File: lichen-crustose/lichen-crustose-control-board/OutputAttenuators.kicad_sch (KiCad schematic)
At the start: 10 parts, among them J7 Thonkiconn_Mono_Audio_Jack, J8 Thonkiconn_Mono_Audio_Jack

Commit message: Updates Lichen symbols and footprints. Fixes to Crustose and Vactrol VCA. Adds 3D model of the RP2350 dual USB board.
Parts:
- J7, J8, RV9: now left out of the parts list
- R33, R34: value 10k_0603 -> 1k_0603; JLCPCB ID C25804 -> (none)
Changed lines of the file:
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@@
 			)
 		)
-		(property "Datasheet" ""
+		(property "Datasheet" "https://jlcpcb.com/api/file/downloadByFileSystemAccessId/8579706381320323072"
 			(at 91.44 82.55 0)
 			(effects
@@
 		(unit 1)
 		(exclude_from_sim no)
-		(in_bom yes)
+		(in_bom no)
 		(on_board yes)
 		(dnp no)
@@
 			)
 		)
-		(property "Value" "10k_0603"
+		(property "Value" "1k_0603"
 			(at 97.79 133.35 90)
 			(effects
@@
 			)
 		)
-		(property "JLCPCB ID" "C25804"
-			(at 113.03 137.16 0)
-			(effects
-				(font
-					(size 1.27 1.27)
-				)
-				(hide yes)
-			)
-		)
 		(property "LCSC" "C21190"
 			(at 115.824 137.16 0)
@@
 		(unit 1)
 		(exclude_from_sim no)
-		(in_bom yes)
+		(in_bom no)
 		(on_board yes)
 		(dnp no)
@@
 			)
 		)
-		(property "Datasheet" ""
+		(property "Datasheet" "https://jlcpcb.com/api/file/downloadByFileSystemAccessId/8579706381320323072"
 			(at 91.44 123.19 0)
 			(effects
@@
 		(unit 1)
 		(exclude_from_sim no)
-		(in_bom yes)
+		(in_bom no)
 		(on_board yes)
 		(dnp no)
@@
 			)
 		)
-		(property "Value" "10k_0603"
+		(property "Value" "1k_0603"
 			(at 96.52 92.71 90)
 			(effects
@@
 			)
 		)
-		(property "JLCPCB ID" "C25804"
-			(at 111.76 96.52 0)
-			(effects
-				(font
-					(size 1.27 1.27)
-				)
-				(hide yes)
-			)
-		)

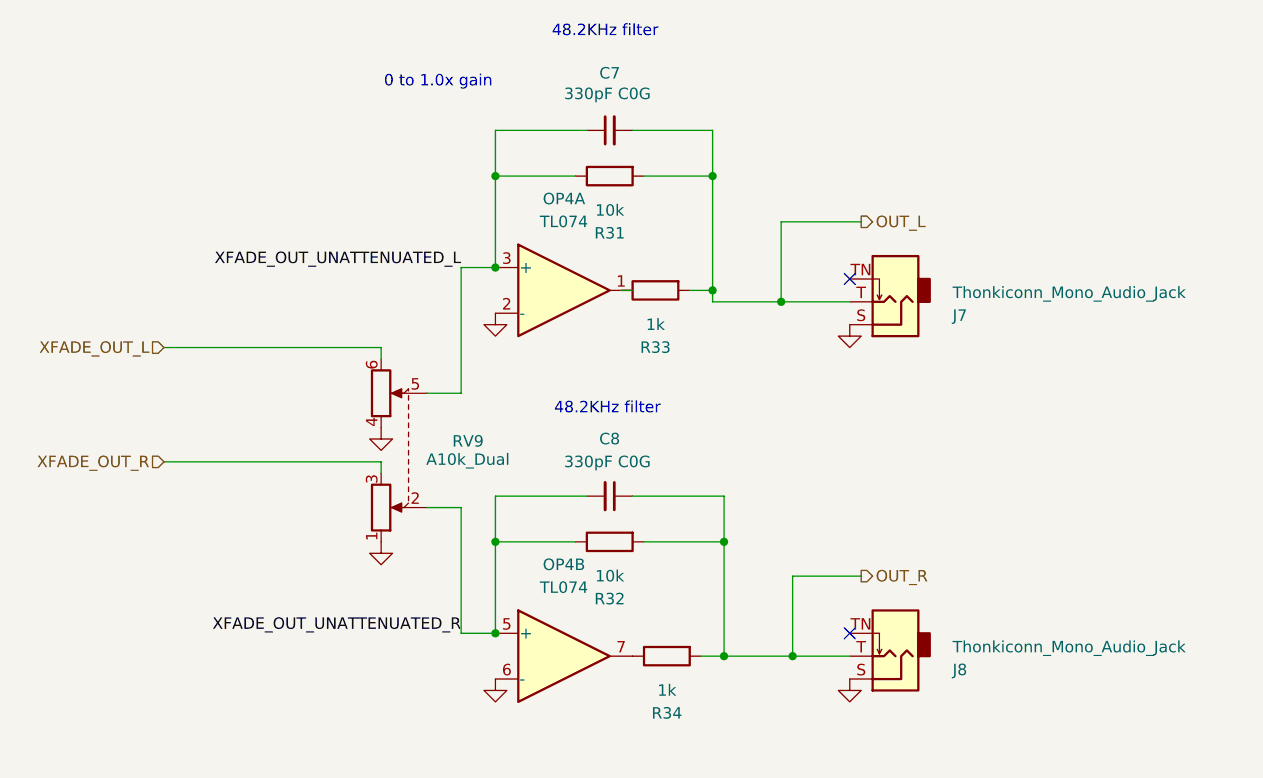
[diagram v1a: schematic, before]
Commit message: feat: Updates Crustose, Cladonia and YouMe Transformer. Adds Stereo Latencies.
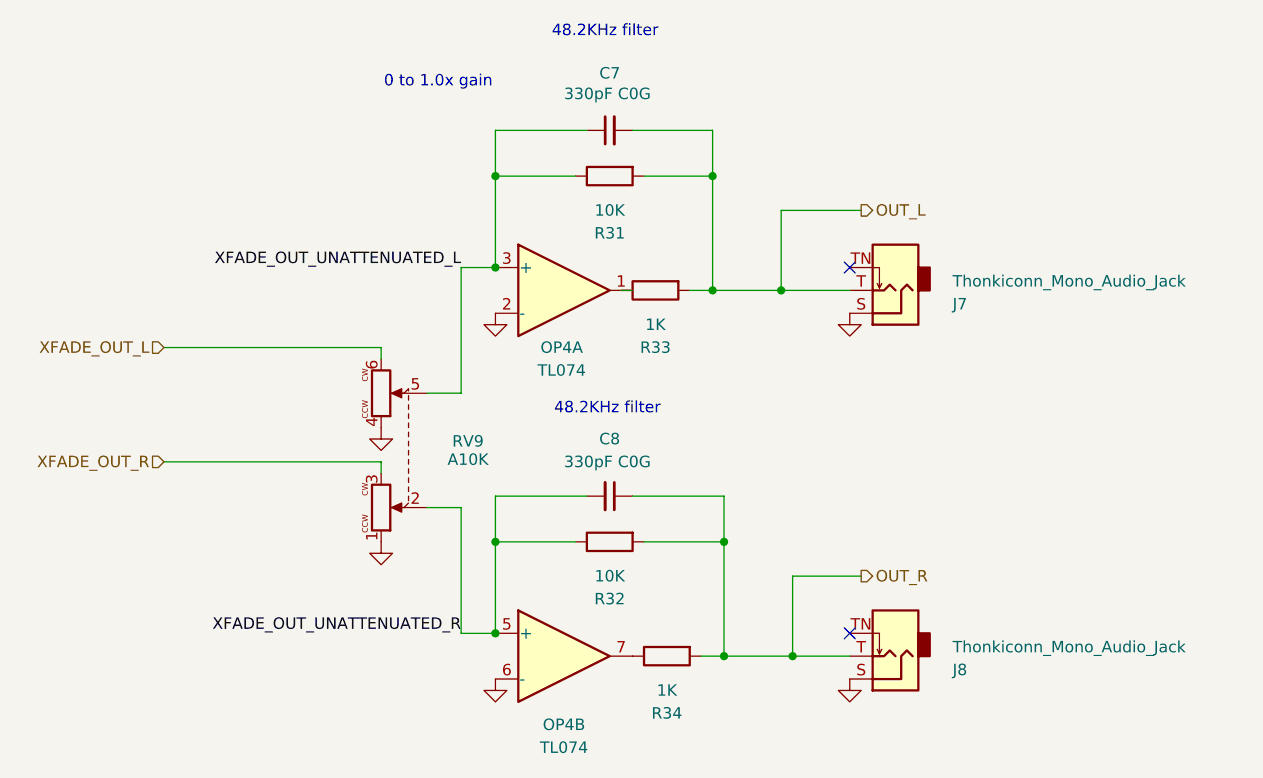
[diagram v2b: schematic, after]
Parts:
- C7, C8: Specifications 330pF 50V C0G ±5% 0603 MLCC -> (none)
- OP4: symbol Amplifier_Operational:TL074 -> Lichen:TL074; LCSC (none) -> C6964; Manufacturer (none) -> Texas Instruments; Part Number (none) -> TL074IDR
- R31, R32: value 10k_0603 -> 10K; Display 10k -> 10K; JLCPCB ID C25804 -> (none); LCSC (none) -> C25804
- R33, R34: value 1k_0603 -> 1K; Display 1k -> 1K
- RV9: value A10k_Dual -> A10K; symbol Lichen:10K_Potentiometer_Dual_Gang_Alpha_RD902F -> Lichen:R_Potentiometer_Dual
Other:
- moved on the sheet: J7
